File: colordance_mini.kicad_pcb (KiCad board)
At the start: 2 copper layers, 174 x 123 mm, 71 parts, among them J1 XLR3, J10 CONN_01X06, J11 CONN_01X04, J12 CONN_01X04, J13 CONN_01X03, J14 CONN_01X03, J15 CONN_01X03, J16 CONN_01X03, J17 CONN_01X04, J2 CONN_01X08, J3 CONN_01X04, J4 CONN_01X03, J5 CONN_01X04, J6 CONN_01X03, J7 CONN_01X04, J8 CONN_01X04, J9 CONN_01X04, SW1 Rotary_Encoder, SW2 Rotary_Encoder, SW3 Rotary_Encoder, SW4 Rotary_Encoder, U1 MAX485CSA+, U2 ROE-0505S, U3 6N137, U4 Teensy3.5

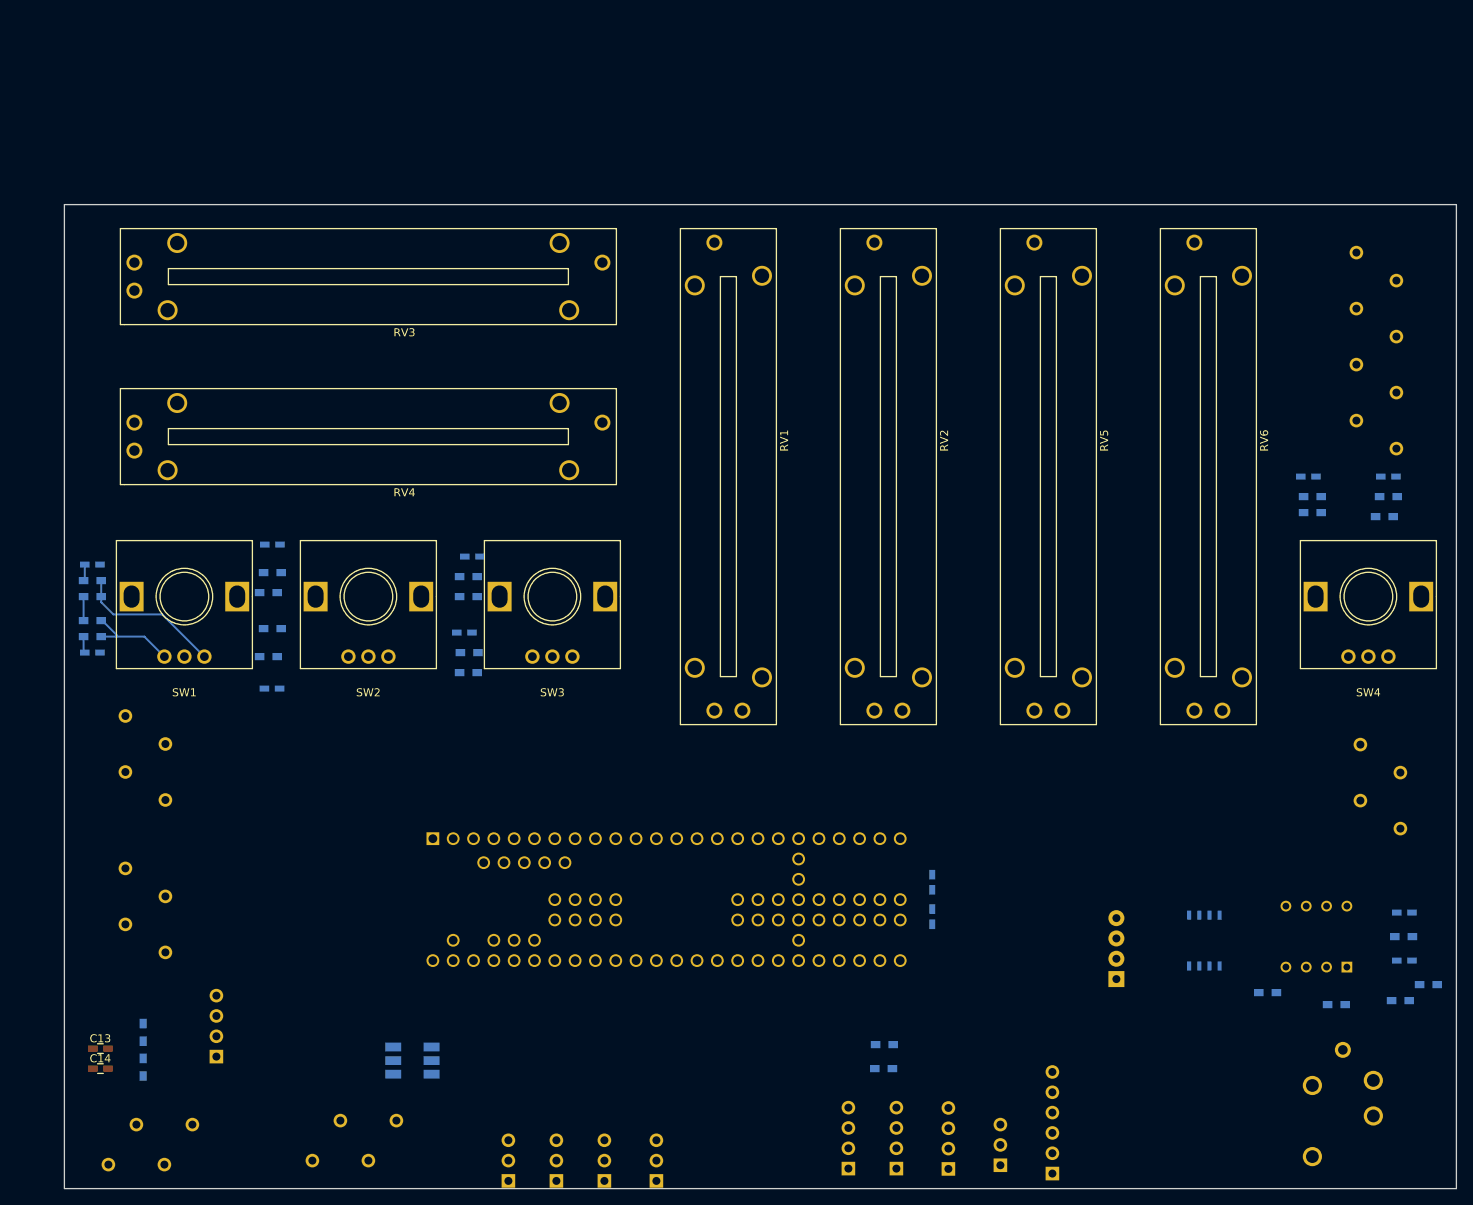
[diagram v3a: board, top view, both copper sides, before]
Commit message: Add mounting holes
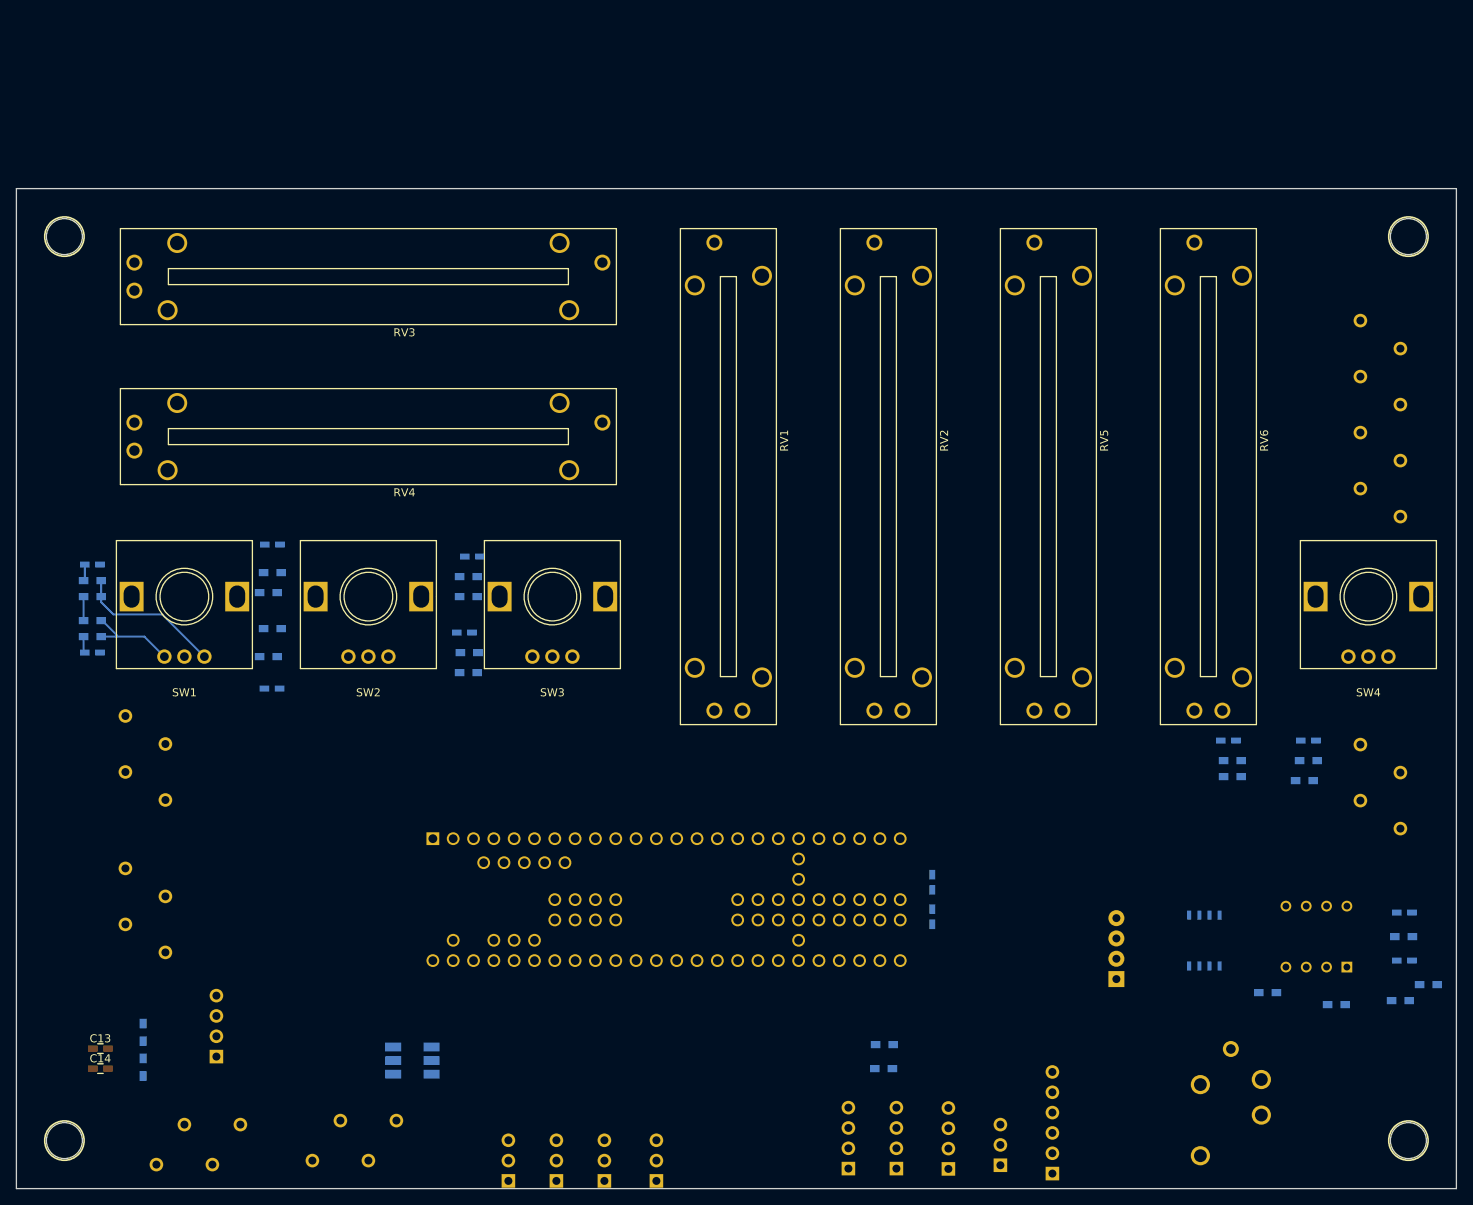
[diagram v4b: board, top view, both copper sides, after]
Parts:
- added H1: HOLE, homebrew:HOLE_M4, F.Cu at (195.0, 158.0)
- added H2: HOLE, homebrew:HOLE_M4, F.Cu at (27.0, 45.0)
- added H3: HOLE, homebrew:HOLE_M4, F.Cu at (27.0, 158.0)
- added H4: HOLE, homebrew:HOLE_M4, F.Cu at (195.0, 45.0)
- moved C10 34.5 mm to (182.5, 108.0)
- moved C6 34.5 mm to (172.5, 108.0)
- moved R15 34.5 mm to (173.0, 112.5)
- moved R17 34.5 mm to (173.0, 110.5)
- moved R19 34.5 mm to (182.5, 110.5)
- moved R21 34.5 mm to (182.0, 113.0)
- moved J1 14.0 mm to (172.8, 146.6)
- moved J2 8.51 mm to (194.0, 80.0)
- moved J4 6.00 mm to (38.5, 161.0)
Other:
- board size 174 x 123 mm -> 180 x 125 mm
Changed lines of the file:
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@@
   (general
     (links 179)
-    (no_connects 170)
-    (area 0 0 0 0)
+    (no_connects 172)
+    (area 26.949999 40.949999 201.050001 164.050001)
     (thickness 1.6)
     (drawings 9)
     (tracks 16)
     (zones 0)
-    (modules 71)
+    (modules 75)
     (nets 103)
   )
@@
   )
   (module Capacitors_SMD:C_0603_HandSoldering (layer B.Cu)
-    (at 182.5 75)
+    (at 172.5 108)
     (descr "Capacitor SMD 0603, hand soldering")
     (tags "capacitor 0603")
@@
   )
   (module Capacitors_SMD:C_0603_HandSoldering (layer B.Cu)
-    (at 192.5 75)
+    (at 182.5 108)
     (descr "Capacitor SMD 0603, hand soldering")
     (tags "capacitor 0603")
@@
   )
   (module homebrew:1985250_phoenix_8pos_3.5mm (layer B.Cu)
-    (at 193.5 71.5 270)
+    (at 194 80 270)
     (fp_text reference J2 (at -13.5 8.5 270) (layer B.SilkS)
       (effects (font (size 1 1) (thickness 0.15)) (justify mirror))
@@
   )
   (module homebrew:1985218_phoenix_4pos_3.5mm (layer B.Cu)
-    (at 32.5 161 180)
+    (at 38.5 161 180)
     (fp_text reference J4 (at -0.255001 -5.847325 180) (layer B.SilkS)
       (effects (font (size 1 1) (thickness 0.15)) (justify mirror))
@@
   )
   (module Resistors_SMD:R_0603_HandSoldering (layer B.Cu)
-    (at 183 79.5)
+    (at 173 112.5)
     (descr "Resistor SMD 0603, hand soldering")
     (tags "resistor 0603")
@@
   )
   (module Resistors_SMD:R_0603_HandSoldering (layer B.Cu)
-    (at 183 77.5)
+    (at 173 110.5)
     (descr "Resistor SMD 0603, hand soldering")
     (tags "resistor 0603")
@@
   )
   (module Resistors_SMD:R_0603_HandSoldering (layer B.Cu)
-    (at 192.5 77.5)
+    (at 182.5 110.5)
     (descr "Resistor SMD 0603, hand soldering")
     (tags "resistor 0603")
@@
   )
   (module Resistors_SMD:R_0603_HandSoldering (layer B.Cu)
-    (at 192 80)
+    (at 182 113)
     (descr "Resistor SMD 0603, hand soldering")
     (tags "resistor 0603")
@@
   )
   (module homebrew:NC3FAH (layer B.Cu)
-    (at 186.81 146.66)
+    (at 172.81 146.55)
     (fp_text reference J1 (at 0 -7.75) (layer B.SilkS)
       (effects (font (size 1 1) (thickness 0.15)) (justify mirror))
@@
     (pad "" thru_hole circle (at 3.81 8.26) (size 2.4 2.4) (drill 1.6) (layers *.Cu *.Mask))
   )
-  (gr_line (start 27 164) (end 27 41) (layer Edge.Cuts) (width 0.1))
-  (gr_line (start 201 164) (end 27 164) (layer Edge.Cuts) (width 0.1))
-  (gr_line (start 201 41) (end 201 164) (layer Edge.Cuts) (width 0.1))
-  (gr_line (start 27 41) (end 201 41) (layer Edge.Cuts) (width 0.1))
+  (module homebrew:HOLE_M4 (layer F.Cu)
+    (at 195 158)
+    (fp_text reference H1 (at 0 4.25) (layer F.SilkS) hide
+      (effects (font (size 1 1) (thickness 0.15)))
+    )
+    (fp_text value HOLE (at 0 -4.5) (layer F.Fab) hide
+      (effects (font (size 1 1) (thickness 0.15)))
+    )
+    (fp_circle (center 0 0) (end 1 2.25) (layer F.SilkS) (width 0.2))
+    (fp_circle (center 0 0) (end 0 3) (layer F.CrtYd) (width 0.15))
+    (fp_circle (center 0 0) (end 0 3) (layer B.CrtYd) (width 0.15))
+    (pad "" np_thru_hole circle (at 0 0) (size 4.5 4.5) (drill 4.5) (layers *.Cu *.Mask)
+      (solder_mask_margin 0.1))
+  )
+  (module homebrew:HOLE_M4 (layer F.Cu)
+    (at 27 45)
+    (fp_text reference H2 (at 0 4.25) (layer F.SilkS) hide
+      (effects (font (size 1 1) (thickness 0.15)))
+    )
+    (fp_text value HOLE (at 0 -4.5) (layer F.Fab) hide
+      (effects (font (size 1 1) (thickness 0.15)))
+    )
+    (fp_circle (center 0 0) (end 1 2.25) (layer F.SilkS) (width 0.2))
+    (fp_circle (center 0 0) (end 0 3) (layer F.CrtYd) (width 0.15))
+    (fp_circle (center 0 0) (end 0 3) (layer B.CrtYd) (width 0.15))
+    (pad "" np_thru_hole circle (at 0 0) (size 4.5 4.5) (drill 4.5) (layers *.Cu *.Mask)
+      (solder_mask_margin 0.1))
+  )
+  (module homebrew:HOLE_M4 (layer F.Cu)
+    (at 27 158)
+    (fp_text reference H3 (at 0 4.25) (layer F.SilkS) hide
+      (effects (font (size 1 1) (thickness 0.15)))
+    )
+    (fp_text value HOLE (at 0 -4.5) (layer F.Fab) hide
+      (effects (font (size 1 1) (thickness 0.15)))
+    )
+    (fp_circle (center 0 0) (end 1 2.25) (layer F.SilkS) (width 0.2))
+    (fp_circle (center 0 0) (end 0 3) (layer F.CrtYd) (width 0.15))
+    (fp_circle (center 0 0) (end 0 3) (layer B.CrtYd) (width 0.15))
+    (pad "" np_thru_hole circle (at 0 0) (size 4.5 4.5) (drill 4.5) (layers *.Cu *.Mask)
+      (solder_mask_margin 0.1))
+  )
+  (module homebrew:HOLE_M4 (layer F.Cu)
+    (at 195 45)
+    (fp_text reference H4 (at 0 4.25) (layer F.SilkS) hide
+      (effects (font (size 1 1) (thickness 0.15)))
+    )
+    (fp_text value HOLE (at 0 -4.5) (layer F.Fab) hide
+      (effects (font (size 1 1) (thickness 0.15)))
+    )
+    (fp_circle (center 0 0) (end 1 2.25) (layer F.SilkS) (width 0.2))
+    (fp_circle (center 0 0) (end 0 3) (layer F.CrtYd) (width 0.15))
+    (fp_circle (center 0 0) (end 0 3) (layer B.CrtYd) (width 0.15))
+    (pad "" np_thru_hole circle (at 0 0) (size 4.5 4.5) (drill 4.5) (layers *.Cu *.Mask)
+      (solder_mask_margin 0.1))
+  )
+  (gr_line (start 21 164) (end 21 39) (layer Edge.Cuts) (width 0.1))
+  (gr_line (start 201 164) (end 21 164) (layer Edge.Cuts) (width 0.1))
+  (gr_line (start 201 39) (end 201 164) (layer Edge.Cuts) (width 0.1))
+  (gr_line (start 21 39) (end 201 39) (layer Edge.Cuts) (width 0.1))
   (gr_text Logger (at 56 144) (layer B.SilkS)
     (effects (font (size 1.5 1.5) (thickness 0.3)) (justify mirror))

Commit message: Placement finished
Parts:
- moved C7 42.7 mm to (153.5, 141.5)
- moved C8 41.2 mm to (153.5, 139.5)
- moved R23 32.8 mm to (165.0, 118.0), turned to 0 degrees
- moved R22 32.5 mm to (165.0, 137.0), turned to 180 degrees
- moved R4 29.0 mm to (165.0, 139.0)
- moved R1 28.3 mm to (165.0, 122.0), turned to 180 degrees
- moved R5 23.1 mm to (165.0, 120.0)
- moved U1 15.6 mm to (157.5, 123.0)
- moved R16 6.58 mm to (76.5, 93.0)
- moved U3 5.39 mm to (181.5, 127.5)
- moved C10 5.15 mm to (180.0, 112.5)
- moved J12 5.00 mm to (120.0, 161.6)
- moved C12 4.94 mm to (137.5, 125.5)
- moved C6 4.74 mm to (174.0, 112.5)
- moved J8 4.63 mm to (30.0, 105.0)
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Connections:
- U2 pad 1: (no net) -> GND
- U2 pad 2: (no net) -> +5V
- U2 pad 3: (no net) -> GND
- U2 pad 4: (no net) -> VDMX

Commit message: Routing finished
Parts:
- C13, C14: moved to B.Cu
- moved D1 41.8 mm to (45.0, 116.0), turned to 0 degrees
- moved C11 34.8 mm to (170.0, 121.0), turned to 180 degrees
- moved C12 33.1 mm to (170.0, 119.0), turned to 180 degrees
- moved R24 17.5 mm to (112.0, 158.5)
- moved R25 17.5 mm to (112.0, 160.5)
- moved U1 12.8 mm to (168.5, 129.5)
- moved J12 7.50 mm to (127.5, 161.5)
- moved J11 7.50 mm to (120.0, 161.6)
- moved R2 4.54 mm to (37.0, 149.0)
- moved R3 4.33 mm to (37.0, 144.5)
- moved C7 3.72 mm to (156.5, 139.3), turned to 180 degrees
- moved C8 3.47 mm to (156.5, 141.3), turned to 180 degrees
- moved U2 3.00 mm to (156.2, 132.0), turned to 0 degrees
- moved C13 2.26 mm to (32.2, 148.6), turned to 180 degrees
- moved C14 2.26 mm to (32.2, 151.1), turned to 180 degrees
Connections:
- C13 pad 2: Net-(C13-Pad2) -> GND
- C14 pad 2: Net-(C13-Pad2) -> GND
- J5 pad 2: +5V -> +3V3
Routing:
- net +5V: track 0.00 -> 264.4 mm, vias 0 -> 8
- net PREV_EFFECT_LED: track 0.00 -> 201.9 mm, vias 0 -> 2
- net PARAM: track 0.00 -> 186.7 mm, vias 0 -> 4
- net DENSITY: track 0.00 -> 172.9 mm, vias 0 -> 4
- net NEXT_EFFECT_LED: track 0.00 -> 169.9 mm, vias 0 -> 2
- net PAN: track 0.00 -> 165.0 mm, vias 0 -> 2
- net HEIGHT: track 0.00 -> 159.6 mm, vias 0 -> 4
- net TILT: track 0.00 -> 149.2 mm, vias 0 -> 4
- net NEXT_EFFECT: track 0.00 -> 144.0 mm, vias 0 -> 1
- net WIDTH: track 0.00 -> 143.8 mm, vias 0 -> 2
- net ORIENTATION_LED: track 0.00 -> 134.8 mm, vias 0 -> 3
- net PREV_EFFECT: track 0.00 -> 125.0 mm, vias 0 -> 1
- net TEMPO_TAP_LED: track 0.00 -> 120.1 mm, vias 0 -> 3
- net ON_BUTTON_LED: track 0.00 -> 116.5 mm, vias 0 -> 2
- net SERIAL_LOG_OUT: track 0.00 -> 116.3 mm, vias 0 -> 2
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- added copper zone on F.Cu, net +3V3
- added copper zone on B.Cu, net GND
